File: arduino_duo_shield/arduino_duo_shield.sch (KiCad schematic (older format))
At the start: 19 parts, among them P1 Digital, P10 CONN_01X01, P11 CONN_01X01, P12 CONN_01X01, P13 CONN_01X01, P2 Power, P3 Analog, P4 Analog, P5 PWM, P6 PWM, P7 Communication, P8 CONN_01X01, P9 CONN_01X01

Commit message: Add labels and footprints
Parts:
- removed J? (x6): Conn_01x03_Female, symbol Connector:Conn_01x03_Female
- added J1: Conn_02x07_Counter_Clockwise, Connector_PinHeader_2.54mm:PinHeader_2x07_P2.54mm_Vertical, symbol Connector_Generic:Conn_02x07_Counter_Clockwise
- added J2: Conn_01x02_Male, Connector_PinHeader_2.54mm:PinHeader_1x02_P2.54mm_Vertical, symbol Connector:Conn_01x02_Male
- added J3, J4, J5, J6: Conn_02x03_Counter_Clockwise, Connector_PinHeader_2.54mm:PinHeader_2x03_P2.54mm_Vertical, symbol Connector_Generic:Conn_02x03_Counter_Clockwise
- added JP1: Jumper_3_Bridged12, Connector_PinHeader_2.54mm:PinHeader_1x03_P2.54mm_Vertical, symbol Jumper:Jumper_3_Bridged12
- added K1: G5Q-1, Relay_THT:Relay_SPDT_Omron-G5Q-1, symbol Relay:G5Q-1
- added Q1, Q2: IRFZ44N, Package_TO_SOT_THT:TO-220-3_Vertical, symbol Device:Q_NMOS_GDS
- added U1, U2: 4504, Package_DIP:DIP-16_W7.62mm, symbol 4xxx:4504
- renumbered P8 to P1, P1 to P10, P5 to P11, P6 to P12, P7 to P13, P9 to P2, P10 to P3, P11 to P4, P12 to P5, P13 to P6, P2 to P7, P3 to P8, P4 to P9
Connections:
- net labels added: +24V, PWR, Probe, VREF+, Xmn, Xmx, Ymn, Ymx, Zmn, Zmx, m1dir, m1enab, m1step, m2dir, m2enab, m2step, m3dir, m3enab, m3step, m4dir, m4enab, m4step, spenab, sppwm
- wire segments 132 -> 249
- no-connect marks 7 -> 63
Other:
- moved on the sheet: P1, P10, P11, P12, P13, P2, P3, P4, P5, P6, P7, P8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

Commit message: Replace 4x 6x connectors with 1x 24x, add firmware
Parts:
- removed J1: Conn_02x07_Counter_Clockwise, Connector_PinHeader_2.54mm:PinHeader_2x07_P2.54mm_Vertical, symbol Connector_Generic:Conn_02x07_Counter_Clockwise
- removed J3, J4, J5, J6: Conn_02x03_Counter_Clockwise, Connector_PinHeader_2.54mm:PinHeader_2x03_P2.54mm_Vertical, symbol Connector_Generic:Conn_02x03_Counter_Clockwise
- added C8: 100pF, Capacitor_THT:C_Disc_D5.0mm_W2.5mm_P2.50mm, symbol Device:C_Small
- added D1: DIODE, Diode_THT:D_A-405_P7.62mm_Horizontal, symbol pspice:DIODE
- added J1: Conn_02x07_Odd_Even, Connector_PinHeader_2.54mm:PinHeader_2x07_P2.54mm_Vertical, symbol Connector_Generic:Conn_02x07_Odd_Even
- added J3: Conn_02x12_Odd_Even, Connector_PinHeader_2.54mm:PinHeader_2x12_P2.54mm_Horizontal, symbol Connector_Generic:Conn_02x12_Odd_Even
- Q1, Q2: value IRFZ44N -> IRLZ44N
- U1, U2: footprint Package_DIP:DIP-16_W7.62mm -> Package_DIP:DIP-16_W7.62mm_Socket
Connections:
- wire segments 249 -> 269
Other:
- moved on the sheet: J2, K1, P1, P10, P11, P12, P13, P2, P3, P4, P5, P6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

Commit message: Fixed power pins
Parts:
- removed J1: Conn_02x07_Odd_Even, Connector_PinHeader_2.54mm:PinHeader_2x07_P2.54mm_Vertical, symbol Connector_Generic:Conn_02x07_Odd_Even
- removed Q1, Q2: IRLZ44N, Package_TO_SOT_THT:TO-220-3_Vertical, symbol Device:Q_NMOS_GDS
- added J4: Limit_Switches, Connector_PinHeader_2.54mm:PinHeader_2x07_P2.54mm_Vertical, symbol Connector_Generic:Conn_01x14
- added Q1: 2N7000, Package_TO_SOT_THT:TO-92_Inline, symbol Transistor_FET:2N7000
- added Q2: BS250, Package_TO_SOT_THT:TO-92_Inline, symbol Transistor_FET:BS250
- added Q3, Q4: IRLZ44N, Package_TO_SOT_THT:TO-220-3_Vertical, symbol Transistor_FET:IRLZ44N
- added R14, R15: 10K, Resistor_THT:R_Axial_DIN0204_L3.6mm_D1.6mm_P2.54mm_Vertical, symbol Device:R
- J3: value Conn_02x12_Odd_Even -> Motor_Control
- JP1: symbol Jumper:Jumper_3_Bridged12 -> sw_spdt:SW_SPDT
- P7: symbol Connector_Generic:Conn_01x08 -> conn_01x08_arduino_power:Conn_01x08_arduino_power
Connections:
- wire segments 269 -> 257
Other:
- note removed: "Shield for Arduino Mega Rev 3"
- moved on the sheet: C8, D1, J2, K1

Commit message: Use only 1 VPOW in spindle control
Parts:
- removed C8: 100pF, Capacitor_THT:C_Disc_D5.0mm_W2.5mm_P2.50mm, symbol Device:C_Small
- removed D1: DIODE, Diode_THT:D_A-405_P7.62mm_Horizontal, symbol pspice:DIODE
- removed J2: Conn_01x02_Male, Connector_PinHeader_2.54mm:PinHeader_1x02_P2.54mm_Vertical, symbol Connector:Conn_01x02_Male
- removed K1: G5Q-1, Relay_THT:Relay_SPDT_Omron-G5Q-1, symbol Relay:G5Q-1
- removed Q1: 2N7000, Package_TO_SOT_THT:TO-92_Inline, symbol Transistor_FET:2N7000
- removed Q2: BS250, Package_TO_SOT_THT:TO-92_Inline, symbol Transistor_FET:BS250
- removed Q3, Q4: IRLZ44N, Package_TO_SOT_THT:TO-220-3_Vertical, symbol Transistor_FET:IRLZ44N
- removed R14, R15: 10K, Resistor_THT:R_Axial_DIN0204_L3.6mm_D1.6mm_P2.54mm_Vertical, symbol Device:R
- J3: footprint Connector_PinHeader_2.54mm:PinHeader_2x12_P2.54mm_Horizontal -> Connector_PinHeader_2.54mm:PinHeader_2x12_P2.54mm_Vertical
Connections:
- net labels removed: +24V, PWR
- wire segments 257 -> 229
- no-connect marks 63 -> 62

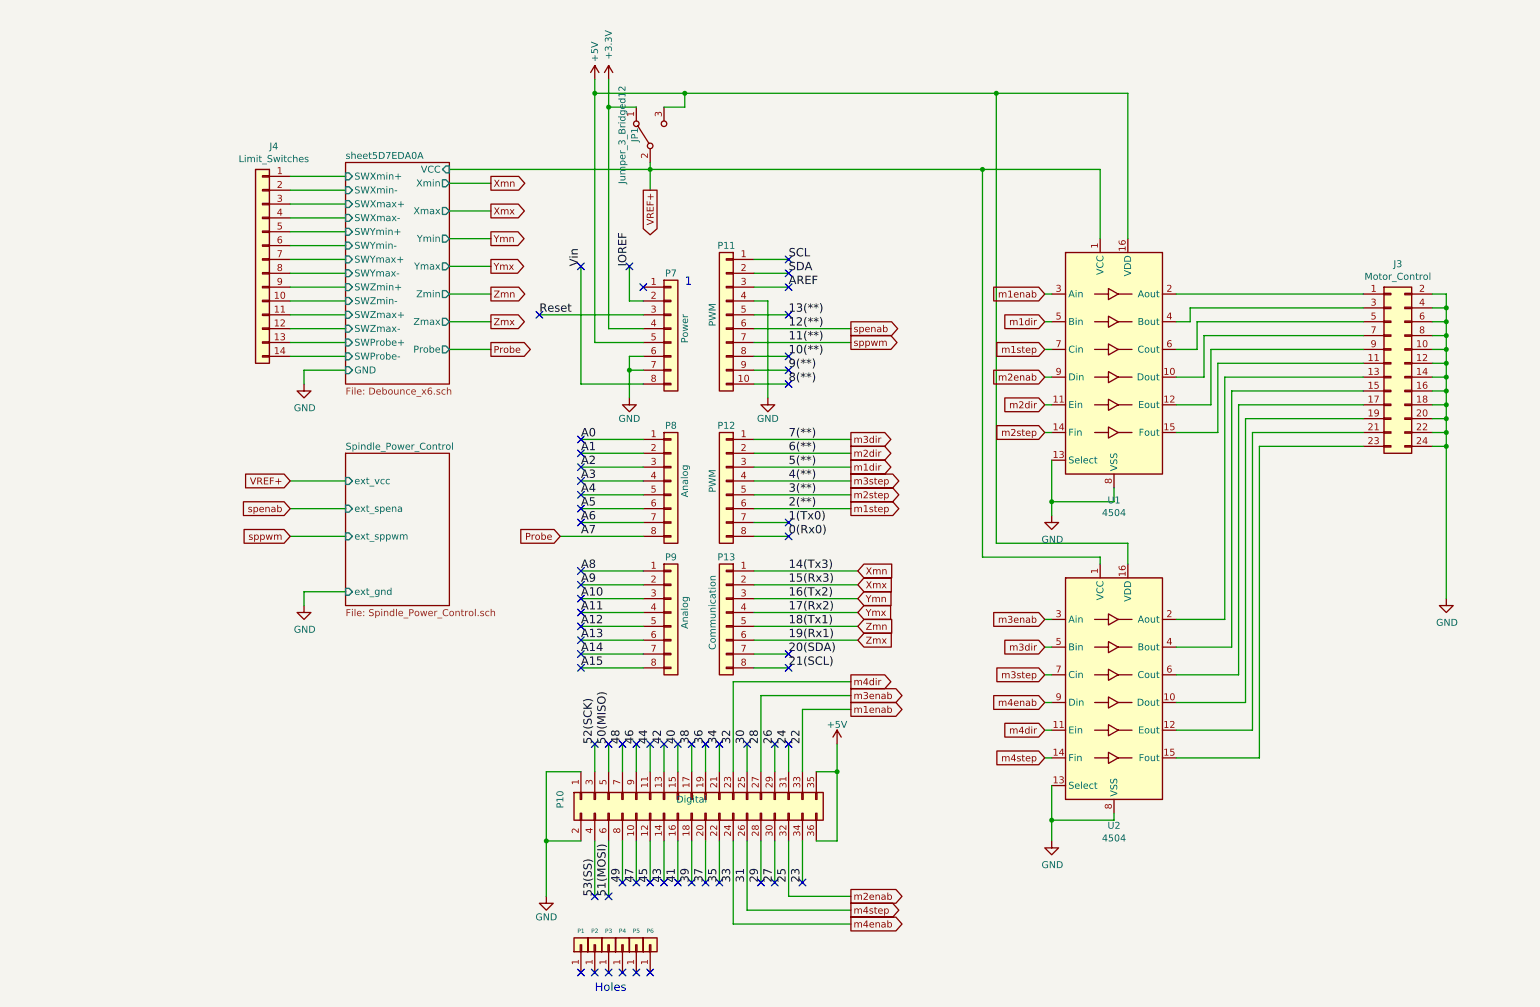
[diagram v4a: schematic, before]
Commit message: Power block to PCB
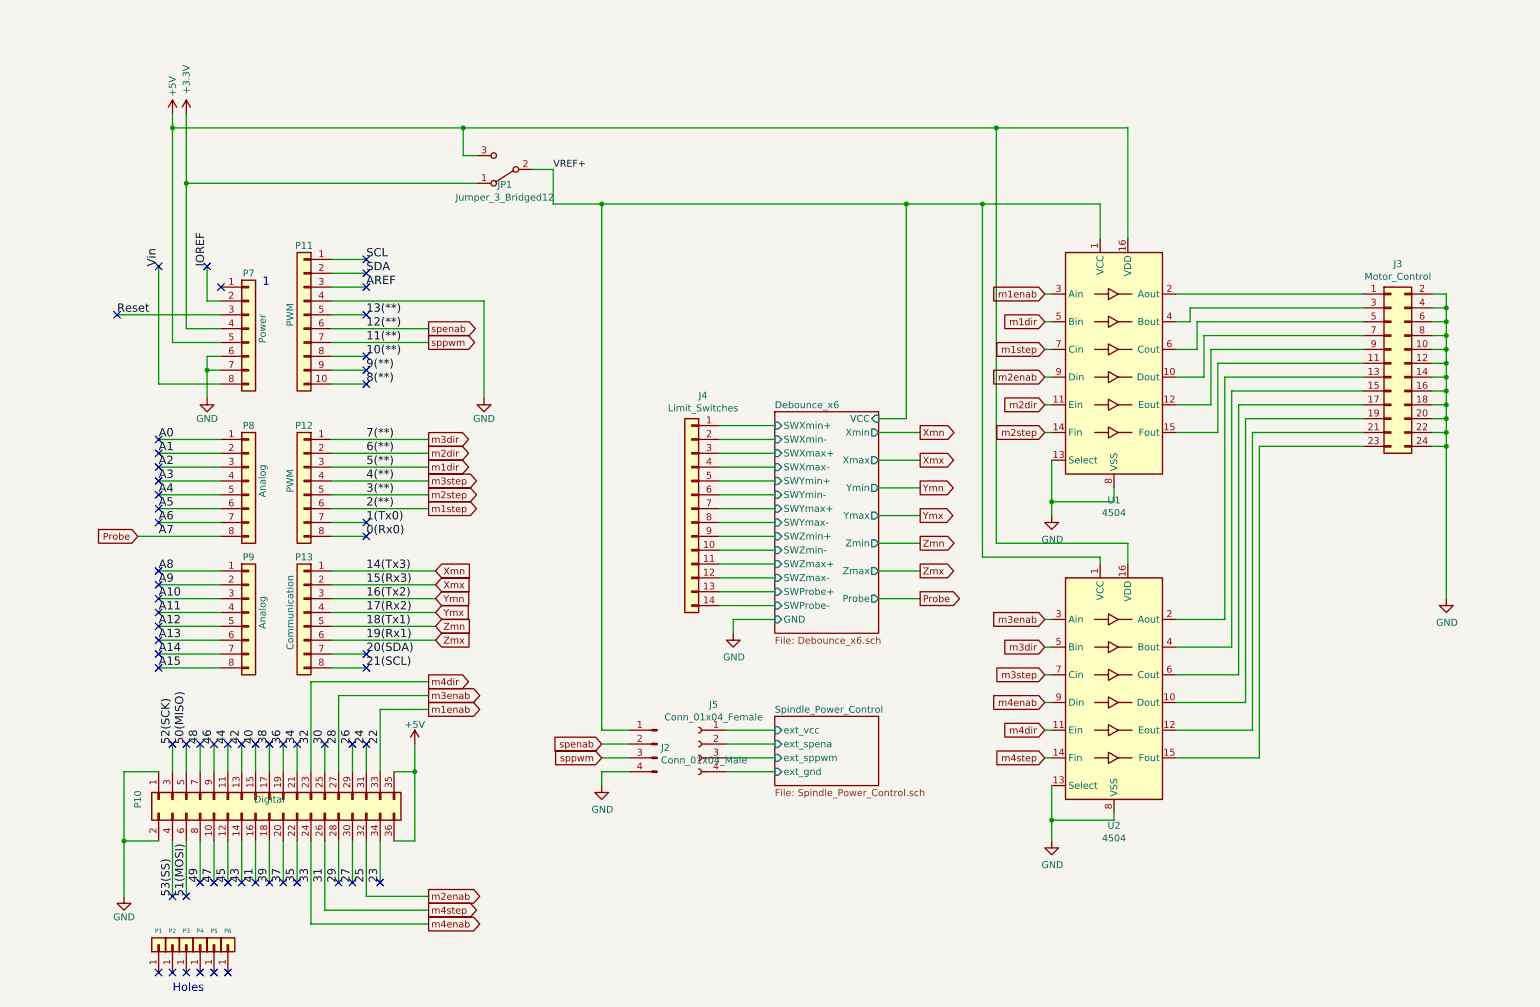
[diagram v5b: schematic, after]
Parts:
- added J2: Conn_01x04_Male, Connector_PinHeader_2.54mm:PinHeader_1x04_P2.54mm_Vertical, symbol Connector:Conn_01x04_Male
- added J5: Conn_01x04_Female, TerminalBlock_RND:TerminalBlock_RND_205-00278_1x04_P5.00mm_Vertical, symbol Connector:Conn_01x04_Female
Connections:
- net GND: now also J2.4 (Pin_4)
- net VREF+: now also J2.1 (Pin_1)
- net spenab: now also J2.2 (Pin_2)
- net sppwm: now also J2.3 (Pin_3)
- net sheet5D7EDA0A/SWProbe+ renamed Debounce_x6/SWProbe+
- net sheet5D7EDA0A/SWProbe- renamed Debounce_x6/SWProbe-
- net sheet5D7EDA0A/SWXmax+ renamed Debounce_x6/SWXmax+
- net sheet5D7EDA0A/SWXmax- renamed Debounce_x6/SWXmax-
- net sheet5D7EDA0A/SWXmin+ renamed Debounce_x6/SWXmin+
- net sheet5D7EDA0A/SWXmin- renamed Debounce_x6/SWXmin-
- net sheet5D7EDA0A/SWYmax+ renamed Debounce_x6/SWYmax+
- net sheet5D7EDA0A/SWYmax- renamed Debounce_x6/SWYmax-
- net sheet5D7EDA0A/SWYmin+ renamed Debounce_x6/SWYmin+
- net sheet5D7EDA0A/SWYmin- renamed Debounce_x6/SWYmin-
- net sheet5D7EDA0A/SWZmax+ renamed Debounce_x6/SWZmax+
- net sheet5D7EDA0A/SWZmax- renamed Debounce_x6/SWZmax-
- net sheet5D7EDA0A/SWZmin+ renamed Debounce_x6/SWZmin+
- net sheet5D7EDA0A/SWZmin- renamed Debounce_x6/SWZmin-
- new net Spindle_Power_Control/ext_gnd: J5.4 (Pin_4)
- new net Spindle_Power_Control/ext_spena: J5.2 (Pin_2)
- new net Spindle_Power_Control/ext_sppwm: J5.3 (Pin_3)
- new net Spindle_Power_Control/ext_vcc: J5.1 (Pin_1)
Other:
- moved on the sheet: J4, JP1, P1, P10, P11, P12, P13, P2, P3, P4, P5, P6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

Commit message: Add PCB front/back for spindle controls
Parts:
- added J6: Spindle_Signal, TerminalBlock:TerminalBlock_bornier-2_P5.08mm, symbol Connector:Conn_01x02_Female
- J2: value Conn_01x04_Male -> Spindle_Control
- J5: value Conn_01x04_Female -> Spindle_Relay_Power; footprint TerminalBlock_RND:TerminalBlock_RND_205-00278_1x04_P5.00mm_Vertical -> TerminalBlock:TerminalBlock_bornier-2_P5.08mm; symbol Connector:Conn_01x04_Female -> Connector:Conn_01x02_Female
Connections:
- net Spindle_Power_Control/ext_spena is gone; now on net Spindle_Power_Control/ext_gnd: J5.2 (Pin_2)
- net Spindle_Power_Control/ext_gnd: no longer J5.4 (Pin_4)
- net Spindle_Power_Control/ext_sppwm: now also J6.2 (Pin_2); no longer J5.3 (Pin_3)
- net VREF+: now also J2.3 (Pin_3); no longer J2.1 (Pin_1)
- net spenab: now also J2.1 (Pin_1); no longer J2.2 (Pin_2)
- net sppwm: now also J2.2 (Pin_2); no longer J2.3 (Pin_3)
- new net Spindle_Power_Control/ext_spenab: J6.1 (Pin_1)
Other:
- moved on the sheet: J2
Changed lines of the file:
@@
 Text GLabel 1350 4100 0    50   Input ~ 0
 Probe
-Text GLabel 4700 5600 0    50   Input ~ 0
+Text GLabel 4900 5500 0    50   Input ~ 0
 spenab
-Text GLabel 4700 5700 0    50   Input ~ 0
+Text GLabel 4900 5600 0    50   Input ~ 0
 sppwm
 $Comp
 L power:GND #PWR01
 U 1 1 5D91A1FA
-P 4700 5900
-F 0 "#PWR01" H 4700 5650 50  0001 C CNN
-F 1 "GND" H 4705 5727 50  0000 C CNN
-F 2 "" H 4700 5900 50  0001 C CNN
-F 3 "" H 4700 5900 50  0001 C CNN
-	1    4700 5900
+P 4350 5900
+F 0 "#PWR01" H 4350 5650 50  0001 C CNN
+F 1 "GND" H 4355 5727 50  0000 C CNN
+F 2 "" H 4350 5900 50  0001 C CNN
+F 3 "" H 4350 5900 50  0001 C CNN
+	1    4350 5900
 	1    0    0    -1
 $EndComp
 Wire Wire Line
 	5600 5600 5950 5600
-Wire Wire Line
-	5600 5500 5950 5500
-$Comp
-L Connector:Conn_01x04_Female J5
-U 1 1 5D974B94
-P 5400 5600
-F 0 "J5" H 5292 5885 50  0000 C CNN
-F 1 "Conn_01x04_Female" H 5292 5794 50  0000 C CNN
-F 2 "TerminalBlock_RND:TerminalBlock_RND_205-00278_1x04_P5.00mm_Vertical" H 5400 5600 50  0001 C CNN
-F 3 "~" H 5400 5600 50  0001 C CNN
-	1    5400 5600
-	-1   0    0    -1
-$EndComp
 $Comp
 L Connector:Conn_01x04_Male J2
 U 1 1 5D975AD3
-P 5100 5600
-F 0 "J2" H 5072 5574 50  0000 R CNN
-F 1 "Conn_01x04_Male" H 5072 5483 50  0000 R CNN
-F 2 "Connector_PinHeader_2.54mm:PinHeader_1x04_P2.54mm_Vertical" H 5100 5600 50  0001 C CNN
-F 3 "~" H 5100 5600 50  0001 C CNN
-	1    5100 5600
+P 5300 5600
+F 0 "J2" H 5272 5574 50  0000 R CNN
+F 1 "Spindle_Control" H 5272 5483 50  0000 R CNN
+F 2 "Connector_PinHeader_2.54mm:PinHeader_1x04_P2.54mm_Vertical" H 5300 5600 50  0001 C CNN
+F 3 "~" H 5300 5600 50  0001 C CNN
+	1    5300 5600
 	-1   0    0    -1
 $EndComp
@@
 	5600 5800 5950 5800
 Wire Wire Line
-	4900 5800 4700 5800
+	5100 5800 4350 5800
 Wire Wire Line
-	4700 5800 4700 5900
+	4350 5800 4350 5900
 Wire Wire Line
-	4900 5700 4700 5700
+	5100 5600 4900 5600
 Wire Wire Line
-	4900 5600 4700 5600
-Wire Wire Line
-	4900 5500 4700 5500
-$Sheet
-S 5950 5400 750  500
-U 5D7DFDC0
-F0 "Spindle_Power_Control" 50
-F1 "Spindle_Power_Control.sch" 50
-F2 "ext_gnd" I L 5950 5800 50
-F3 "ext_sppwm" I L 5950 5700 50
-F4 "ext_spena" I L 5950 5600 50
-F5 "ext_vcc" I L 5950 5500 50
-$EndSheet
+	5100 5500 4900 5500
 Wire Wire Line
 	1500 5800 1250 5800
@@
 	4350 1450 4350 1700
 Wire Wire Line
-	4350 1700 4700 1700
-Wire Wire Line
-	4700 5500 4700 1700
-Connection ~ 4700 1700
-Wire Wire Line
-	4700 1700 6900 1700
-Wire Wire Line
 	3700 1150 3700 1350
 Wire Wire Line
@@
 Text Label 4350 1450 0    50   ~ 0
 VREF+
+$Sheet
+S 5950 5400 750  500
+U 5D7DFDC0
+F0 "Spindle_Power_Control" 50
+F1 "Spindle_Power_Control.sch" 50
+F2 "ext_gnd" I L 5950 5800 50
+F3 "ext_sppwm" I L 5950 5600 50
+F4 "ext_vcc" I L 5950 5700 50
+F5 "ext_spenab" I L 5950 5500 50
+$EndSheet
+Wire Wire Line
+	4350 1700 6900 1700
+Connection ~ 4350 1700
+Wire Wire Line
+	5100 5700 4350 5700
+Wire Wire Line
+	4350 5700 4350 1700
+Wire Wire Line
+	5600 5500 5950 5500
+$Comp
+L Connector:Conn_01x02_Female J5
+U 1 1 5D974B94
+P 5400 5700
+F 0 "J5" H 5292 5985 50  0000 C CNN
+F 1 "Spindle_Relay_Power" H 5292 5894 50  0000 C CNN
+F 2 "TerminalBlock:TerminalBlock_bornier-2_P5.08mm" H 5400 5700 50  0001 C CNN
+F 3 "~" H 5400 5700 50  0001 C CNN
+	1    5400 5700
+	-1   0    0    -1
+$EndComp
+$Comp
+L Connector:Conn_01x02_Female J6
+U 1 1 5D89B5D7
+P 5400 5500
+F 0 "J6" H 5292 5785 50  0000 C CNN
+F 1 "Spindle_Signal" H 5292 5694 50  0000 C CNN
+F 2 "TerminalBlock:TerminalBlock_bornier-2_P5.08mm" H 5400 5500 50  0001 C CNN
+F 3 "~" H 5400 5500 50  0001 C CNN
+	1    5400 5500
+	-1   0    0    -1
+$EndComp
 $EndSCHEMATC

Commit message: Complete wiring
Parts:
- removed JP1: Jumper_3_Bridged12, Connector_PinHeader_2.54mm:PinHeader_1x03_P2.54mm_Vertical, symbol sw_spdt:SW_SPDT
- removed U1, U2: 4504, Package_DIP:DIP-16_W7.62mm_Socket, symbol 4xxx:4504
- added SW1: SW_Push, Button_Switch_THT:SW_PUSH_6mm, symbol Switch:SW_Push
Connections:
- net VREF+ is gone; now on net +3V3: J2.3 (Pin_3)
- net +5V: no longer P7.5 (Pin_5)
- net GND: now also SW1.1
- net Reset: now also SW1.2
- net Level_Shifter/hi_1_4: now reaches J3.7 (Pin_7)
- net Level_Shifter/hi_1_5: now reaches J3.9 (Pin_9)
- net Level_Shifter/hi_1_6: now reaches J3.11 (Pin_11)
- net Level_Shifter/hi_1_1: now reaches J3.1 (Pin_1)
- net Level_Shifter/hi_1_2: now reaches J3.3 (Pin_3)
- net Level_Shifter/hi_1_3: now reaches J3.5 (Pin_5)
- net Level_Shifter/hi_2_4: now reaches J3.19 (Pin_19)
- net Level_Shifter/hi_2_5: now reaches J3.21 (Pin_21)
- net Level_Shifter/hi_2_6: now reaches J3.23 (Pin_23)
- net Level_Shifter/hi_2_1: now reaches J3.13 (Pin_13)
- net Level_Shifter/hi_2_2: now reaches J3.15 (Pin_15)
- net Level_Shifter/hi_2_3: now reaches J3.17 (Pin_17)
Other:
- moved on the sheet: J3
